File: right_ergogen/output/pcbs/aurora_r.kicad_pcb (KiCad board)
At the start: 2 copper layers, 154 x 114.2 mm, 122 parts

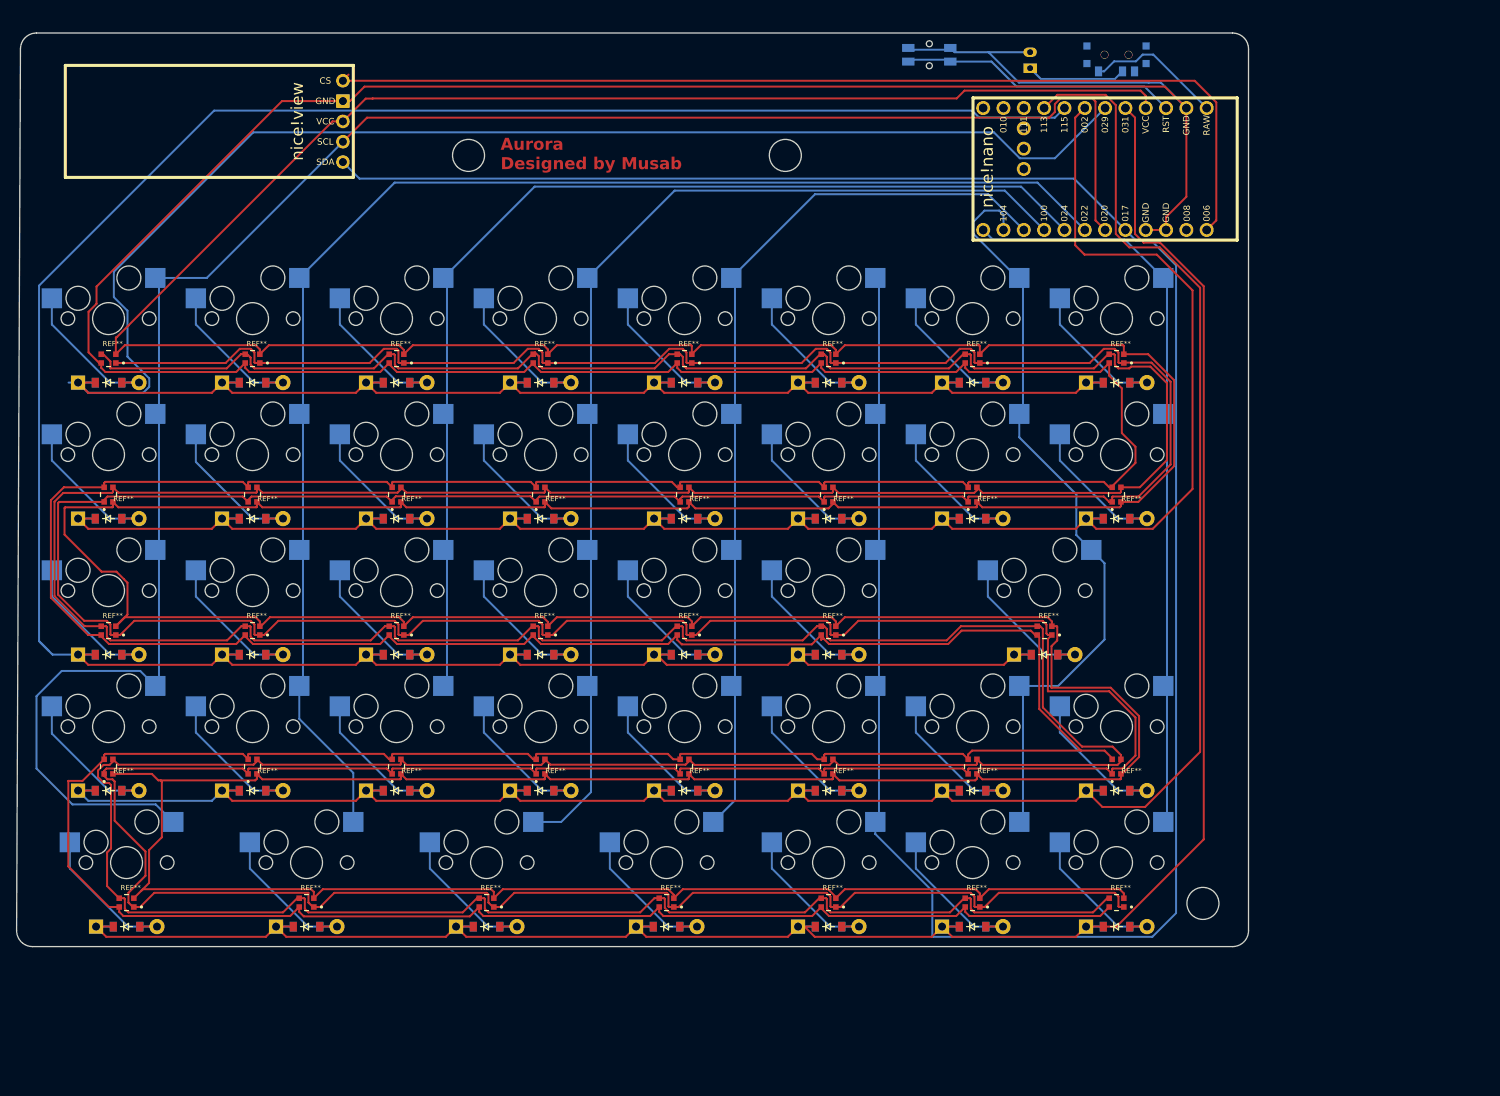
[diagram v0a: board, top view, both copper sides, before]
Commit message: Key clearance fixes and mounting hole placement fixes
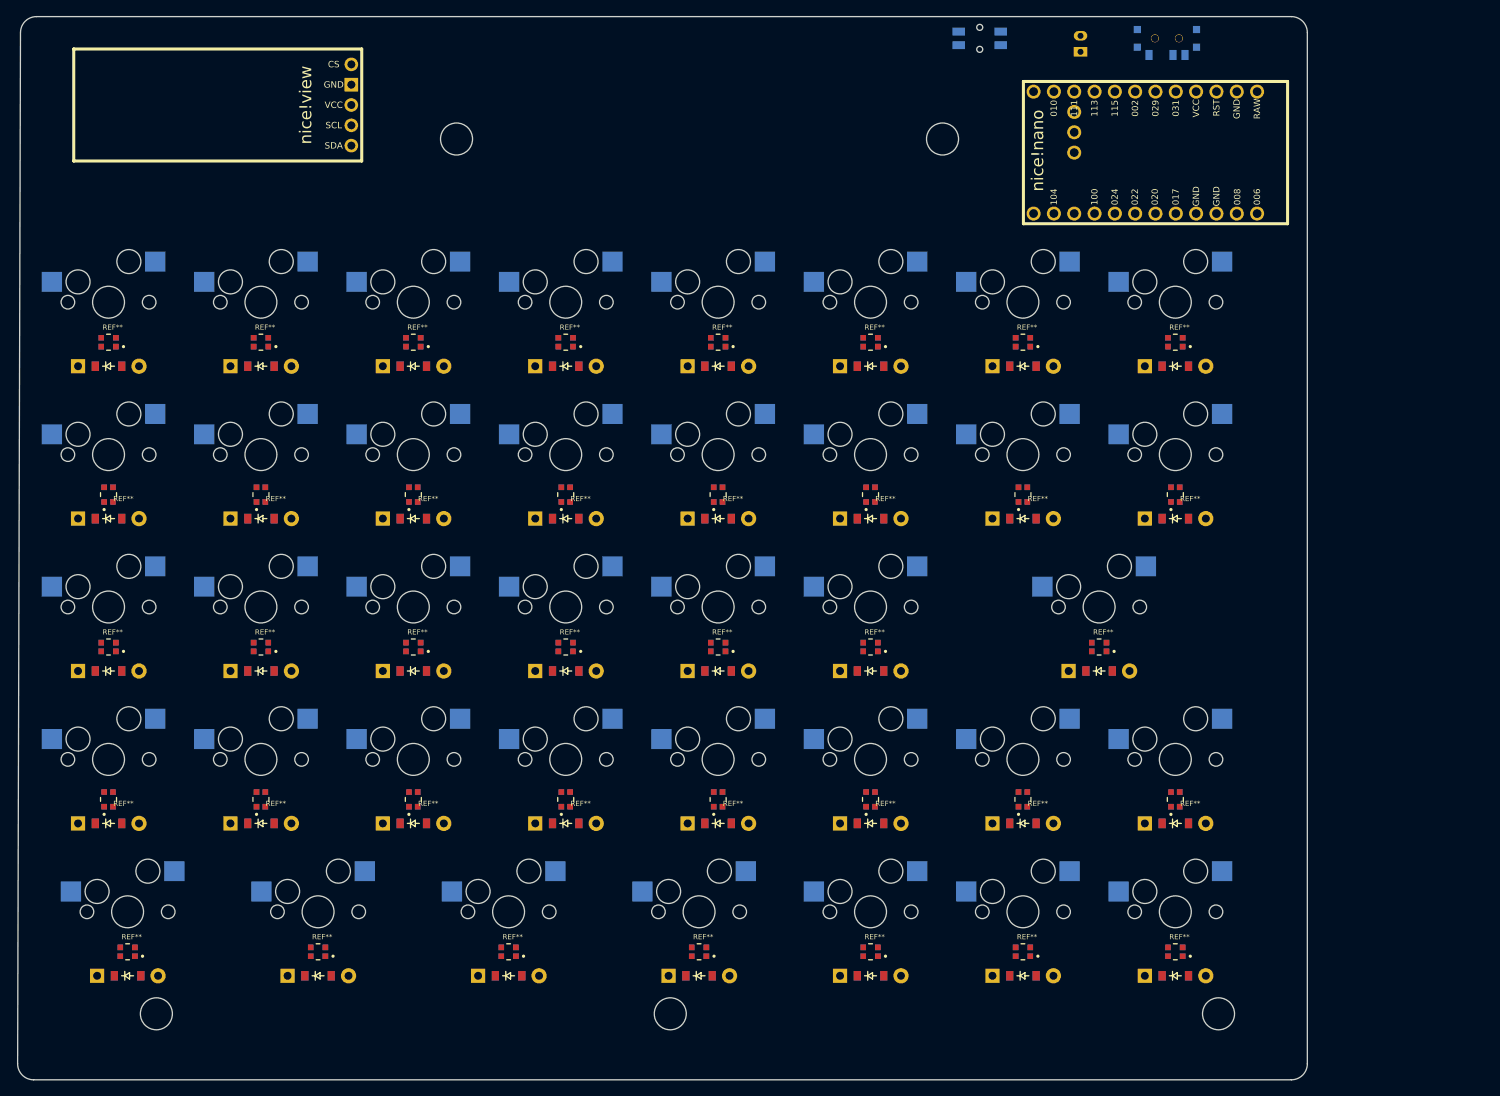
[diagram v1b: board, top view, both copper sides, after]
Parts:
- removed the ? at (184.6, 62.6)
- removed the ? at (236.8, 156.1)
- removed the ? at (145.0, 62.6)
- removed the REF** at (226.0, 88.0)
- removed the REF** at (172.0, 88.0)
- removed the REF** at (217.0, 122.0)
- removed the REF** at (190.0, 88.0)
- removed the REF** at (190.0, 105.0)
- removed the REF** at (208.0, 88.0)
- removed the REF** at (190.0, 139.0)
- removed the REF** at (118.0, 122.0)
- removed the REF** at (124.8, 156.0)
- removed the REF** at (208.0, 156.0)
- removed the REF** at (190.0, 122.0)
- removed the REF** at (154.0, 139.0)
- removed the REF** at (100.0, 88.0)
- removed the REF** at (147.2, 156.0)
- removed the REF** at (154.0, 122.0)
- removed the REF** at (208.0, 105.0)
- removed the REF** at (154.0, 88.0)
- removed the REF** at (100.0, 139.0)
- removed the REF** at (102.2, 156.0)
- removed the REF** at (118.0, 139.0)
- removed the REF** at (169.8, 156.0)
- removed the REF** at (154.0, 105.0)
- removed the REF** at (136.0, 139.0)
- removed the REF** at (100.0, 122.0)
- removed the REF** at (208.0, 139.0)
- removed the REF** at (136.0, 105.0)
- removed the REF** at (172.0, 122.0)
- removed the REF** at (172.0, 105.0)
- removed the REF** at (226.0, 105.0)
- removed the REF** at (118.0, 88.0)
- removed the REF** at (226.0, 156.0)
- removed the REF** at (172.0, 139.0)
- removed the REF** at (136.0, 88.0)
- removed the REF** at (190.0, 156.0)
- removed the REF** at (226.0, 139.0)
- removed the REF** at (136.0, 122.0)
- removed the REF** at (118.0, 105.0)
- added ?: , HOLE_M2_TH, F.Cu at (170.2, 169.9)
- added ?: , HOLE_M2_TH, F.Cu at (143.5, 60.5)
- added ?: , HOLE_M2_TH, F.Cu at (106.0, 169.9)
- added ?: , HOLE_M2_TH, F.Cu at (204.2, 60.5)
- added ?: , HOLE_M2_TH, F.Cu at (238.8, 169.9)
- added REF**: WS2812, WS2812-2020, F.Cu at (100.0, 143.1)
- added REF**: WS2812, WS2812-2020, F.Cu at (157.2, 105.0)
- added REF**: WS2812, WS2812-2020, F.Cu at (176.2, 105.0)
- added REF**: WS2812, WS2812-2020, F.Cu at (119.0, 143.1)
- added REF**: WS2812, WS2812-2020, F.Cu at (176.2, 143.1)
- added REF**: WS2812, WS2812-2020, F.Cu at (195.2, 143.1)
- added REF**: WS2812, WS2812-2020, F.Cu at (157.2, 86.0)
- added REF**: WS2812, WS2812-2020, F.Cu at (173.8, 162.2)
- added REF**: WS2812, WS2812-2020, F.Cu at (138.1, 143.1)
- added REF**: WS2812, WS2812-2020, F.Cu at (100.0, 86.0)
- added REF**: WS2812, WS2812-2020, F.Cu at (214.3, 162.2)
- added REF**: WS2812, WS2812-2020, F.Cu at (233.3, 162.2)
- added REF**: WS2812, WS2812-2020, F.Cu at (214.3, 143.1)
- added REF**: WS2812, WS2812-2020, F.Cu at (157.2, 124.0)
- added REF**: WS2812, WS2812-2020, F.Cu at (195.2, 105.0)
- added REF**: WS2812, WS2812-2020, F.Cu at (214.3, 86.0)
- added REF**: WS2812, WS2812-2020, F.Cu at (157.2, 143.1)
- added REF**: WS2812, WS2812-2020, F.Cu at (150.0, 162.2)
- added REF**: WS2812, WS2812-2020, F.Cu at (176.2, 86.0)
- added REF**: WS2812, WS2812-2020, F.Cu at (214.3, 105.0)
- added REF**: WS2812, WS2812-2020, F.Cu at (119.0, 105.0)
- added REF**: WS2812, WS2812-2020, F.Cu at (195.2, 162.2)
- added REF**: WS2812, WS2812-2020, F.Cu at (233.3, 105.0)
- added REF**: WS2812, WS2812-2020, F.Cu at (138.1, 124.0)
- added REF**: WS2812, WS2812-2020, F.Cu at (233.3, 86.0)
- added REF**: WS2812, WS2812-2020, F.Cu at (102.4, 162.2)
- added REF**: WS2812, WS2812-2020, F.Cu at (138.1, 86.0)
- added REF**: WS2812, WS2812-2020, F.Cu at (119.0, 124.0)
- added REF**: WS2812, WS2812-2020, F.Cu at (119.0, 86.0)
- added REF**: WS2812, WS2812-2020, F.Cu at (233.3, 143.1)
- added REF**: WS2812, WS2812-2020, F.Cu at (126.2, 162.2)
- added REF**: WS2812, WS2812-2020, F.Cu at (195.2, 124.0)
- added REF**: WS2812, WS2812-2020, F.Cu at (195.2, 86.0)
- added REF**: WS2812, WS2812-2020, F.Cu at (223.8, 124.0)
- added REF**: WS2812, WS2812-2020, F.Cu at (100.0, 124.0)
- added REF**: WS2812, WS2812-2020, F.Cu at (176.2, 124.0)
- added REF**: WS2812, WS2812-2020, F.Cu at (138.1, 105.0)
- moved D38 9.58 mm to (233.3, 165.2)
- moved S38 9.58 mm to (233.3, 157.2)
- moved D37 8.80 mm to (214.3, 165.2)
- moved S37 8.80 mm to (214.3, 157.2)
- moved D31 8.42 mm to (233.3, 146.1)
- moved S31 8.42 mm to (233.3, 138.1)
- moved D36 8.09 mm to (195.2, 165.2)
- moved S36 8.09 mm to (195.2, 157.2)
- moved D16 7.63 mm to (233.3, 89.0)
- moved S16 7.63 mm to (233.3, 81.0)
- moved D30 7.52 mm to (214.3, 146.1)
- moved S30 7.52 mm to (214.3, 138.1)
- moved D35 7.37 mm to (173.8, 165.2)
- moved S35 7.37 mm to (173.8, 157.2)
- moved D15 7.35 mm to (233.3, 108.0)
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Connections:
- REF** pad 1: P8 -> VCC
- REF** pad 2: VCC -> P8
- REF** pad 3: P15 -> GND
- REF** pad 4: GND -> P15
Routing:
- net GND: track 962.9 -> 0.00 mm
- net VCC: track 899.6 -> 0.00 mm
- net P8: track 775.2 -> 0.00 mm
- net P15: track 769.0 -> 0.00 mm
- net P115: track 343.1 -> 0.00 mm
- net P029: track 330.2 -> 0.00 mm
- net P017: track 309.0 -> 0.00 mm
- net P113: track 283.5 -> 0.00 mm
- net P031: track 273.3 -> 0.00 mm
- net P002: track 243.4 -> 0.00 mm
- net P020: track 242.1 -> 0.00 mm
- net P022: track 177.5 -> 0.00 mm
- net P100: track 138.0 -> 0.00 mm
- net P024: track 136.8 -> 0.00 mm
- net P006: track 127.8 -> 0.00 mm
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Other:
- board size 154 x 114.2 mm -> 161.2 x 132.9 mm
- board text removed: "Aurora Designed by Musab"

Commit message: Generate output CAD files
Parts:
- removed the ? at (143.5, 60.5)
- removed the ? at (106.0, 169.9)
- removed the ? at (204.2, 60.5)
- removed the ? at (238.8, 169.9)
- removed the REF** at (233.3, 162.2)
- removed the REF** at (223.8, 124.0)
- added ?: , HOLE_M2_TH, F.Cu at (143.5, 60.6)
- added ?: , HOLE_M2_TH, F.Cu at (204.2, 60.6)
- added ?: , HOLE_M2_TH, F.Cu at (106.0, 169.9)
- added ?: , HOLE_M2_TH, F.Cu at (238.8, 169.9)
- added REF**: WS2812, WS2812-2020, F.Cu at (223.8, 124.0)
- added REF**: WS2812, WS2812-2020, F.Cu at (233.4, 162.2)
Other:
- net class Default added: clearance 0.2, trace_width 0.25, via_dia 0.8, via_drill 0.4

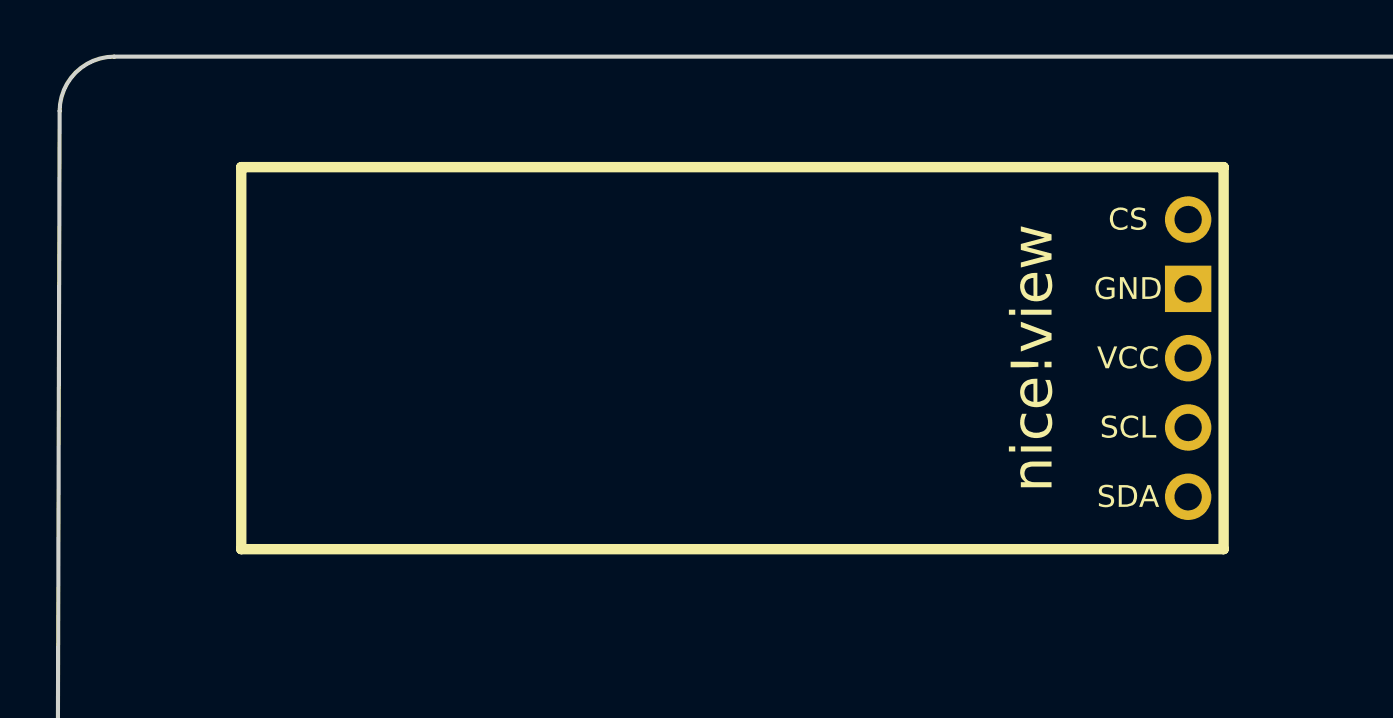
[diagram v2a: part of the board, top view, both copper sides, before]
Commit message: Right PCB dimensioning tweaks
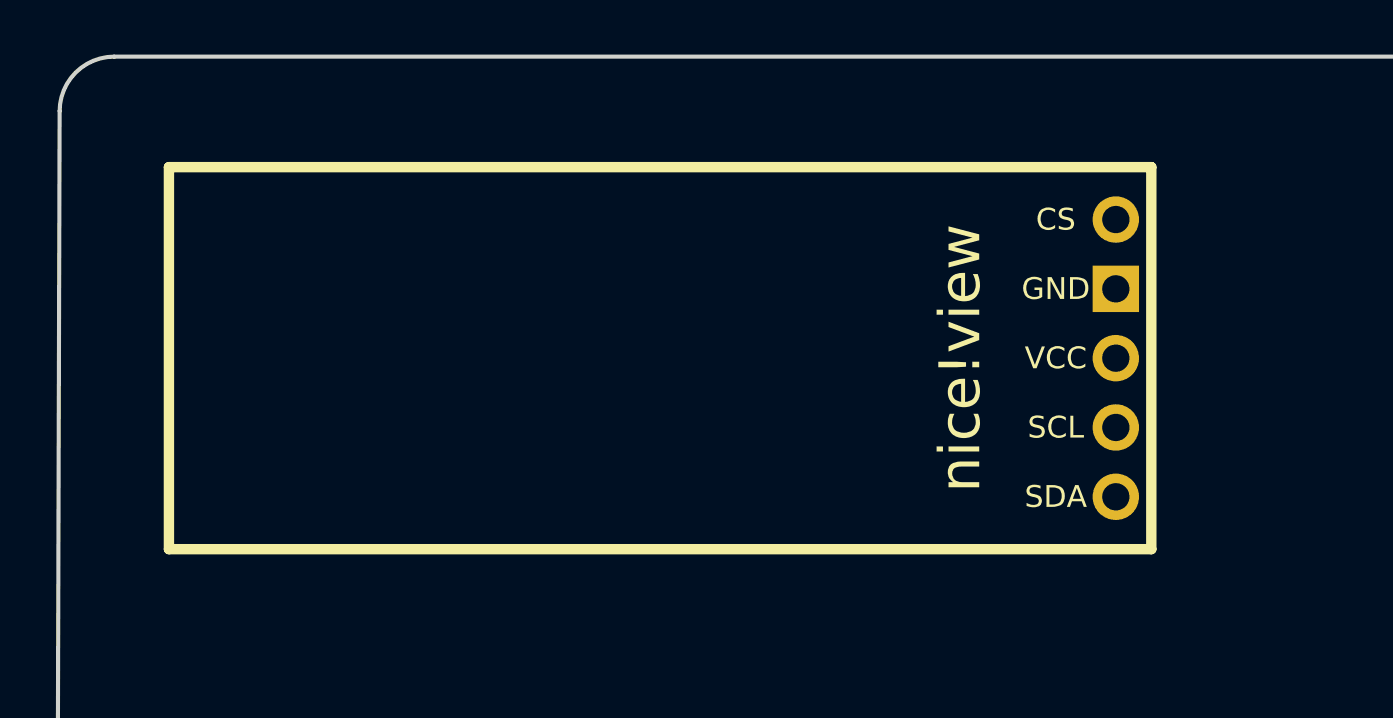
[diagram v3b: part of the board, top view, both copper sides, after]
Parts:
- moved niceView1 2.65 mm to (129.0, 56.3)
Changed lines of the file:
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@@
         )
         (module lib:niceView_headers (layer F.Cu)
-        (at 131.65 56.300000000000004 180)
+        (at 129 56.300000000000004 180)
         (fp_text reference "niceView1" (at 0 0) (layer F.SilkS) hide (effects (font (size 1.27 1.27) (thickness 0.15))))
         (fp_text value niceView (at -1.3 0) (layer F.Fab) hide (effects (font (size 1 1) (thickness 0.15))))
